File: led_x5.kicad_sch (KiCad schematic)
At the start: 5 parts

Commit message: ready to order
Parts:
- D1, D2, D3, D4, D5: footprint LED_SMD:LED_0603_1608Metric -> mark:LED_0603_1608Metric_no_silk
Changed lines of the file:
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@@
       (effects (font (size 1.27 1.27)) (justify right) hide)
     )
-    (property "Footprint" "LED_SMD:LED_0603_1608Metric" (id 2) (at 107.95 70.485 0)
+    (property "Footprint" "mark:LED_0603_1608Metric_no_silk" (id 2) (at 107.95 70.485 0)
       (effects (font (size 1.27 1.27)) hide)
     )
@@
       (effects (font (size 1.27 1.27)) (justify right) hide)
     )
-    (property "Footprint" "LED_SMD:LED_0603_1608Metric" (id 2) (at 107.95 83.185 0)
+    (property "Footprint" "mark:LED_0603_1608Metric_no_silk" (id 2) (at 107.95 83.185 0)
       (effects (font (size 1.27 1.27)) hide)
     )
@@
       (effects (font (size 1.27 1.27)) (justify right) hide)
     )
-    (property "Footprint" "LED_SMD:LED_0603_1608Metric" (id 2) (at 107.95 64.135 0)
+    (property "Footprint" "mark:LED_0603_1608Metric_no_silk" (id 2) (at 107.95 64.135 0)
       (effects (font (size 1.27 1.27)) hide)
     )
@@
   (symbol (lib_id "power:VDD") (at 104.14 83.185 90) (unit 1)
     (in_bom yes) (on_board yes) (fields_autoplaced)
-    (property "Reference" "#PWR058" (id 0) (at 107.95 83.185 0)
+    (property "Reference" "#PWR060" (id 0) (at 107.95 83.185 0)
       (effects (font (size 1.27 1.27)) hide)
     )
@@
       (effects (font (size 1.27 1.27)) (justify right) hide)
     )
-    (property "Footprint" "LED_SMD:LED_0603_1608Metric" (id 2) (at 107.95 76.835 0)
+    (property "Footprint" "mark:LED_0603_1608Metric_no_silk" (id 2) (at 107.95 76.835 0)
       (effects (font (size 1.27 1.27)) hide)
     )
@@
       (effects (font (size 1.27 1.27)) (justify right) hide)
     )
-    (property "Footprint" "LED_SMD:LED_0603_1608Metric" (id 2) (at 107.95 57.785 0)
+    (property "Footprint" "mark:LED_0603_1608Metric_no_silk" (id 2) (at 107.95 57.785 0)
       (effects (font (size 1.27 1.27)) hide)
     )

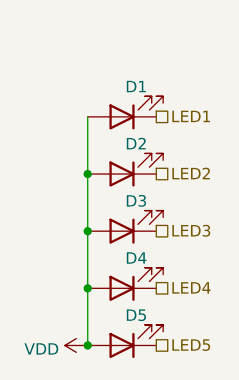
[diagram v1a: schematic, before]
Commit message: started fixing issues from V1
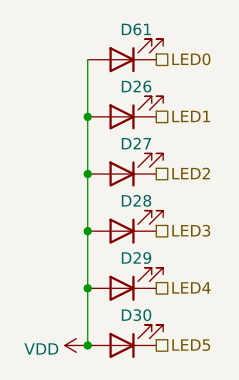
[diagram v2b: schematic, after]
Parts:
- added D61: White, mark:LED_0603_1608Metric_no_silk, symbol Device:LED
- renumbered D1 to D26, D2 to D27, D3 to D28, D4 to D29, D5 to D30
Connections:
- net VDD: now also D61.2 (A)
- new net LED0: D61.1 (K)
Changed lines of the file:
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@@
   (junction (at 104.14 83.185) (diameter 0) (color 0 0 0 0)
+  )
+  (junction (at 104.14 57.785) (diameter 0) (color 0 0 0 0)
   )
   (junction (at 104.14 70.485) (diameter 0) (color 0 0 0 0)
   )
   (junction (at 104.14 64.135) (diameter 0) (color 0 0 0 0)
+  )
+  (wire (pts (xy 104.14 57.785) (xy 104.14 51.435))
+    (stroke (width 0) (type default) (color 0 0 0 0))
   )
   (wire (pts (xy 104.14 83.185) (xy 104.14 76.835))
@@
     (effects (font (size 1.27 1.27)) (justify left))
   )
+  (hierarchical_label "LED0" (shape passive) (at 111.76 51.435 0)
+    (effects (font (size 1.27 1.27)) (justify left))
+  )
   (hierarchical_label "LED5" (shape passive) (at 111.76 83.185 0)
     (effects (font (size 1.27 1.27)) (justify left))
@@
     (effects (font (size 1.27 1.27)) (justify left))
   )
+  (symbol (lib_id "Device:LED") (at 107.95 51.435 180) (unit 1)
+    (in_bom yes) (on_board yes) (fields_autoplaced)
+    (property "Reference" "D61" (id 0) (at 109.5375 48.1132 0))
+    (property "Value" "White" (id 1) (at 111.2397 48.514 90)
+      (effects (font (size 1.27 1.27)) (justify right) hide)
+    )
+    (property "Footprint" "mark:LED_0603_1608Metric_no_silk" (id 2) (at 107.95 51.435 0)
+      (effects (font (size 1.27 1.27)) hide)
+    )
+    (property "Datasheet" "https://datasheet.lcsc.com/lcsc/1809041711_Hubei-KENTO-Elec-C2290_C2290.pdf" (id 3) (at 107.95 51.435 0)
+      (effects (font (size 1.27 1.27)) hide)
+    )
+    (property "JLC" "C2290" (id 4) (at 107.95 51.435 90)
+      (effects (font (size 1.27 1.27)) hide)
+    )
+    (pin "1")
+    (pin "2")
+  )
   (symbol (lib_id "Device:LED") (at 107.95 70.485 180) (unit 1)
     (in_bom yes) (on_board yes) (fields_autoplaced)
-    (property "Reference" "D3" (id 0) (at 109.5375 67.1632 0))
+    (property "Reference" "D28" (id 0) (at 109.5375 67.1632 0))
     (property "Value" "White" (id 1) (at 111.2397 67.564 90)
       (effects (font (size 1.27 1.27)) (justify right) hide)
@@
   (symbol (lib_id "Device:LED") (at 107.95 83.185 180) (unit 1)
     (in_bom yes) (on_board yes) (fields_autoplaced)
-    (property "Reference" "D5" (id 0) (at 109.5375 79.8632 0))
+    (property "Reference" "D30" (id 0) (at 109.5375 79.8632 0))
     (property "Value" "White" (id 1) (at 111.2397 80.264 90)
       (effects (font (size 1.27 1.27)) (justify right) hide)
@@
   (symbol (lib_id "Device:LED") (at 107.95 64.135 180) (unit 1)
     (in_bom yes) (on_board yes) (fields_autoplaced)
-    (property "Reference" "D2" (id 0) (at 109.5375 60.8132 0))
+    (property "Reference" "D27" (id 0) (at 109.5375 60.8132 0))
     (property "Value" "White" (id 1) (at 111.2397 61.214 90)
       (effects (font (size 1.27 1.27)) (justify right) hide)
@@
   (symbol (lib_id "power:VDD") (at 104.14 83.185 90) (unit 1)
     (in_bom yes) (on_board yes) (fields_autoplaced)
-    (property "Reference" "#PWR060" (id 0) (at 107.95 83.185 0)
+    (property "Reference" "#PWR067" (id 0) (at 107.95 83.185 0)
       (effects (font (size 1.27 1.27)) hide)
     )
@@
   (symbol (lib_id "Device:LED") (at 107.95 76.835 180) (unit 1)
     (in_bom yes) (on_board yes) (fields_autoplaced)
-    (property "Reference" "D4" (id 0) (at 109.5375 73.5132 0))
+    (property "Reference" "D29" (id 0) (at 109.5375 73.5132 0))
     (property "Value" "White" (id 1) (at 111.2397 73.914 90)
       (effects (font (size 1.27 1.27)) (justify right) hide)
@@
   (symbol (lib_id "Device:LED") (at 107.95 57.785 180) (unit 1)
     (in_bom yes) (on_board yes) (fields_autoplaced)
-    (property "Reference" "D1" (id 0) (at 109.5375 54.4632 0))
+    (property "Reference" "D26" (id 0) (at 109.5375 54.4632 0))
     (property "Value" "White" (id 1) (at 111.2397 54.864 90)
       (effects (font (size 1.27 1.27)) (justify right) hide)
